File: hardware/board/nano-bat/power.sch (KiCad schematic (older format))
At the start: 26 parts, among them Q501 Q_PMOS_GSD, Q502 Q_NMOS_GSD, Q503 Q_NMOS_GSD, U501 MIC2104YML-TR, U502 MCP1702

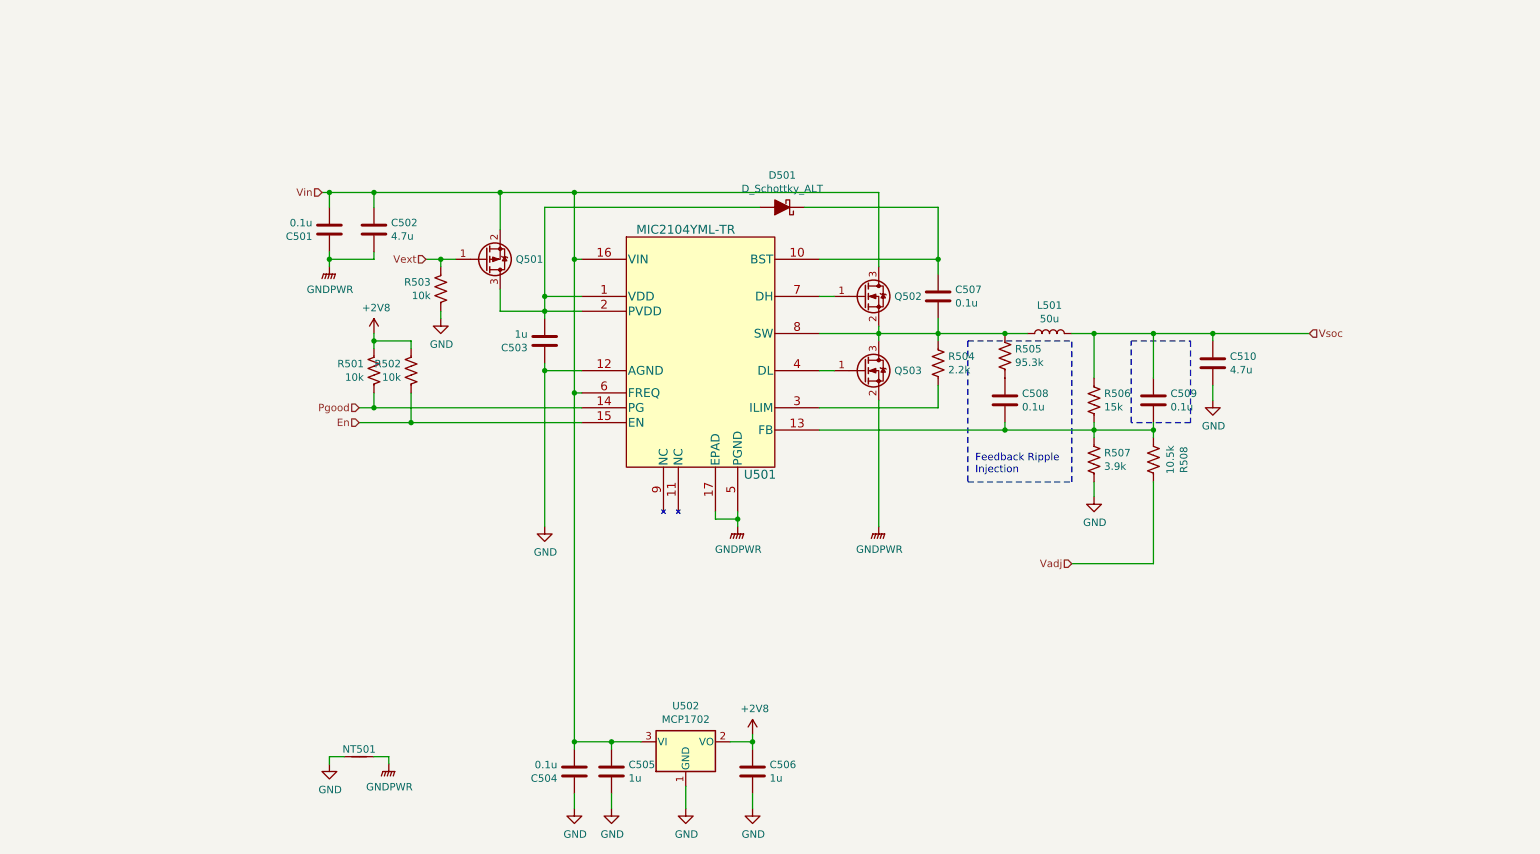
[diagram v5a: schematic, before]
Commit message: Adding docs to schematic
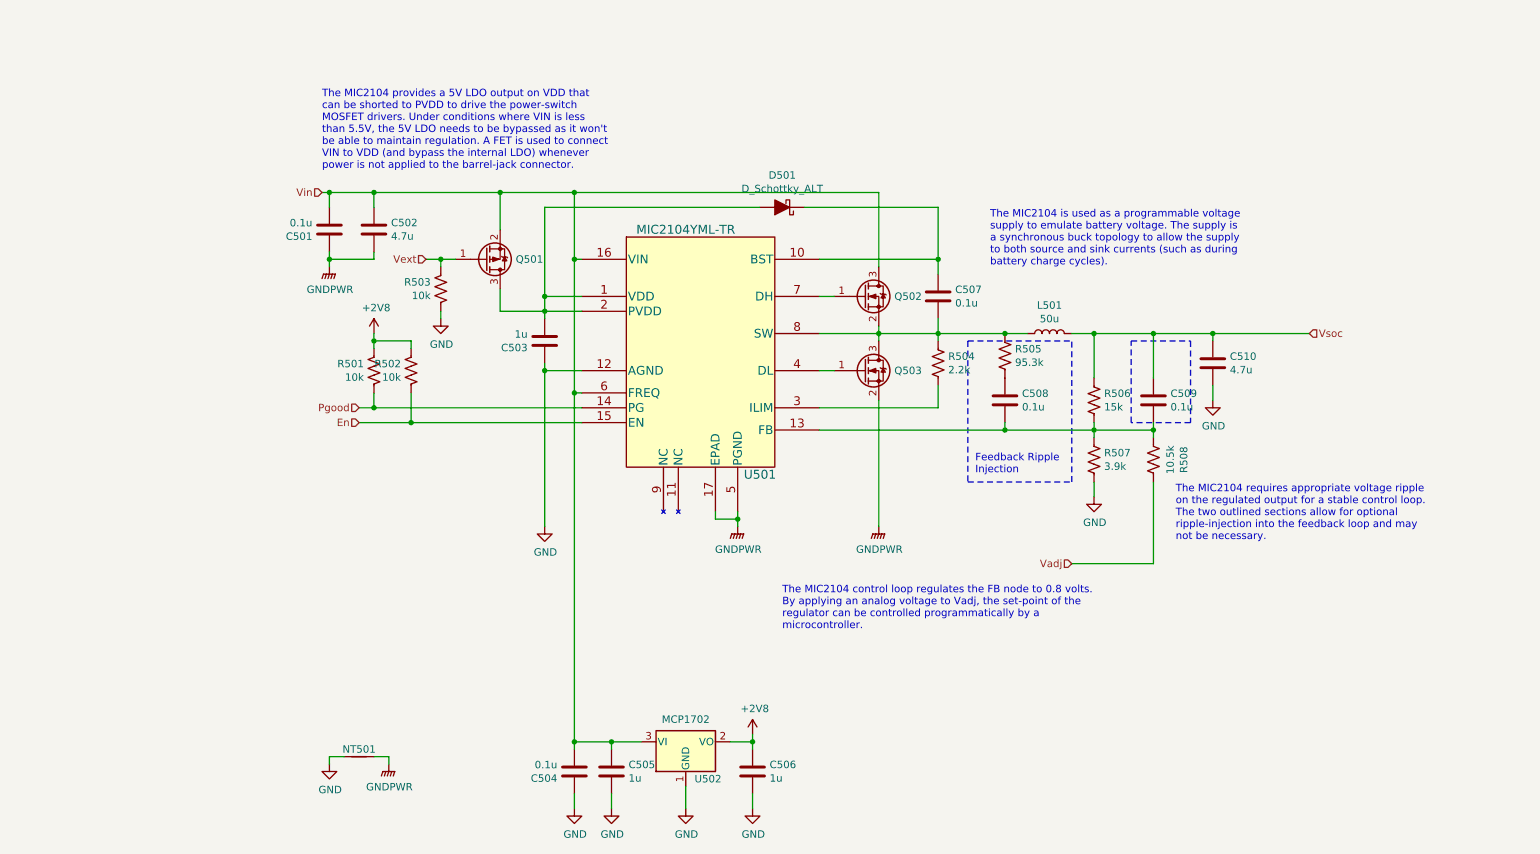
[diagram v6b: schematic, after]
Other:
- note added: "The MIC2104 control loop regulates the FB node to 0.8 volts. \nBy applying an analog voltage to Vadj, the set-point of the \nregulator can be controlled programmatically by a \nmicrocontroller."
- note added: "The MIC2104 is used as a programmable voltage \nsupply to emulate battery voltage. The supply is \na synchronous buck topology to allow the supply \nto both source and sink currents (such as during \nbattery charge cycles)."
- note added: "The MIC2104 provides a 5V LDO output on VDD that \ncan be shorted to PVDD to drive the power-switch \nMOSFET drivers. Under conditions where VIN is less \nthan 5.5V, the 5V LDO needs to be bypassed as it won't \nbe able to maintain regulation. A FET is used to connect \nVIN to VDD (and bypass the internal LDO) whenever \npower is not applied to the barrel-jack connector."
- note added: "The MIC2104 requires appropriate voltage ripple \non the regulated output for a stable control loop. \nThe two outlined sections allow for optional \nripple-injection into the feedback loop and may \nnot be necessary."
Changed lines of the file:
@@
 U 1 1 5DDCE1EA
 P 5400 5750
-F 0 "U502" H 5400 5992 50  0000 C CNN
+F 0 "U502" H 5550 5500 50  0000 C CNN
 F 1 "MCP1702" H 5400 5901 50  0000 C CNN
 F 2 "Package_TO_SOT_SMD:SOT-23" H 5400 5950 50  0001 C CNN
@@
 Wire Wire Line
 	4450 3250 4450 4300
+Text Notes 7450 2550 0    50   ~ 0
+The MIC2104 is used as a programmable voltage \nsupply to emulate battery voltage. The supply is \na synchronous buck topology to allow the supply \nto both source and sink currents (such as during \nbattery charge cycles).
+Text Notes 8700 4400 0    50   ~ 0
+The MIC2104 requires appropriate voltage ripple \non the regulated output for a stable control loop. \nThe two outlined sections allow for optional \nripple-injection into the feedback loop and may \nnot be necessary.
+Text Notes 6050 5000 0    50   ~ 0
+The MIC2104 control loop regulates the FB node to 0.8 volts. \nBy applying an analog voltage to Vadj, the set-point of the \nregulator can be controlled programmatically by a \nmicrocontroller.
+Text Notes 2950 1900 0    50   ~ 0
+The MIC2104 provides a 5V LDO output on VDD that \ncan be shorted to PVDD to drive the power-switch \nMOSFET drivers. Under conditions where VIN is less \nthan 5.5V, the 5V LDO needs to be bypassed as it won't \nbe able to maintain regulation. A FET is used to connect \nVIN to VDD (and bypass the internal LDO) whenever \npower is not applied to the barrel-jack connector.
 $EndSCHEMATC

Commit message: Adding 0.1.0 of board spin
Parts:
- removed C508, C509: 0.1u, Capacitor_SMD:C_0603_1608Metric, symbol Device:C
- removed D501: D_Schottky_ALT, Diode_SMD:D_SOD-323, symbol Device:D_Schottky_ALT
- removed NT501: Net-Tie_2, NetTie:NetTie-2_SMD_Pad2.0mm, symbol Device:Net-Tie_2
- removed Q501: Q_PMOS_GSD, Package_TO_SOT_SMD:SOT-23, symbol Device:Q_PMOS_GSD
- removed Q502, Q503: Q_NMOS_GSD, Package_TO_SOT_SMD:SOT-23, symbol Device:Q_NMOS_GSD
- removed R505: 95.3k, Resistor_SMD:R_0603_1608Metric, symbol Device:R_US
- removed R506: 15k, Resistor_SMD:R_0603_1608Metric, symbol Device:R_US
- removed R507: 3.9k, Resistor_SMD:R_0603_1608Metric, symbol Device:R_US
- removed R508: 10.5k, Resistor_SMD:R_0603_1608Metric, symbol Device:R_US
- removed U501: MIC2104YML-TR, Package_DFN_QFN:QFN-16-1EP_3x3mm_P0.5mm_EP1.7x1.7mm, symbol nano-bat:MIC2104YML-TR
- added F501: Polyfuse, Fuse:Fuse_1812_4532Metric, symbol Device:Polyfuse
- added U501: TPS562201, Package_TO_SOT_SMD:SOT-23-6, symbol Regulator_Switching:TPS562200
- C501, C507: value 0.1u -> 10u; footprint Capacitor_SMD:C_0603_1608Metric -> Capacitor_SMD:C_0805_2012Metric; Part 1276-1258-1-ND -> 399-3482-1-ND
- C502: value 4.7u -> 0.1u; Part 399-3482-1-ND -> 1276-1258-1-ND
- C503: value 1u -> 0.1u; Part 1276-1182-1-ND -> 1276-1258-1-ND
- C510: value 4.7u -> 10u; footprint Capacitor_SMD:C_0603_1608Metric -> Capacitor_SMD:C_0805_2012Metric
- L501: value 50u -> 4.7u; footprint footprints:NRS6028-IND-NS -> Inductor_SMD:L_Taiyo-Yuden_NR-60xx; Part 587-2942-1-ND -> 587-2100-1-ND
- R502: value 10k -> 1.96k; Part 311-10KGRCT-ND -> 311-1.96KHRCT-ND
- R503: value 10k -> 9.31k; Part 311-10KGRCT-ND -> RMCF0603FT9K31CT-ND
- R504: value 2.2k -> 10k; Part P2.2KGCT-ND -> 311-10.0KHRCT-ND
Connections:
- net Pgood is gone; now on net En: R501.2
- net +2V8: no longer R502.1
- net En: now also U501.5 (EN); no longer R502.2
- net GND: now also C501.2, C502.2, C507.2, R502.2, U501.1 (GND); no longer C503.1, R503.2
- net Vadj: now also R503.2
- net Vin: now also C501.1, U501.3 (VIN); no longer C501.2
- net Vsoc: now also F501.1; no longer C510.1, L501.2
- net at C503.2: now also L501.1, U501.2 (SW)
- net at C507.1: now also C510.1, L501.2, R504.2, F501.2
- removed net GNDPWR: C501.1, C502.2
- net Vext: no longer names the net of R503.1
- net Vext: now also R502.1, R504.1, U501.4 (VFB)
- new net: C503.1, U501.6 (VBST)
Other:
- note added: "Vsoc = 5.51 - (1.0741) * Vadj"
- note added: "Vsoc is adjusted to bias VFB to 0.768V. \nVadj is used to change the bias set-point \nthrough external analog control.\n"
- note removed: "Feedback Ripple\nInjection"
- note removed: "The MIC2104 control loop regulates the FB node to 0.8 volts. \nBy applying an analog voltage to Vadj, the set-point of the \nregulator can be controlled programmatically by a \nmicrocontroller."
- note removed: "The MIC2104 is used as a programmable voltage \nsupply to emulate battery voltage. The supply is \na synchronous buck topology to allow the supply \nto both source and sink currents (such as during \nbattery charge cycles)."
- note removed: "The MIC2104 provides a 5V LDO output on VDD that \ncan be shorted to PVDD to drive the power-switch \nMOSFET drivers. Under conditions where VIN is less \nthan 5.5V, the 5V LDO needs to be bypassed as it won't \nbe able to maintain regulation. A FET is used to connect \nVIN to VDD (and bypass the internal LDO) whenever \npower is not applied to the barrel-jack connector."
- note removed: "The MIC2104 requires appropriate voltage ripple \non the regulated output for a stable control loop. \nThe two outlined sections allow for optional \nripple-injection into the feedback loop and may \nnot be necessary."
- moved on the sheet: C510

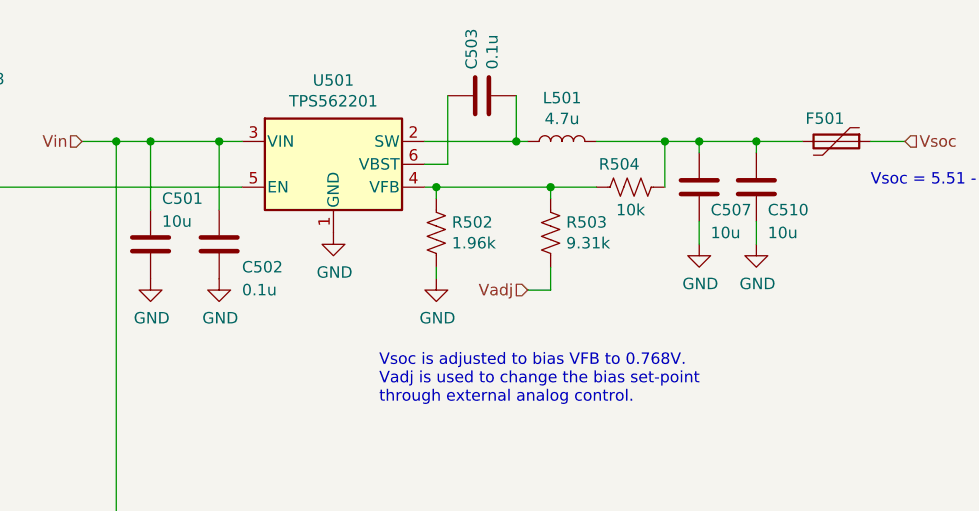
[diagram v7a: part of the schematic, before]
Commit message: Fixing schematic symbol sizes
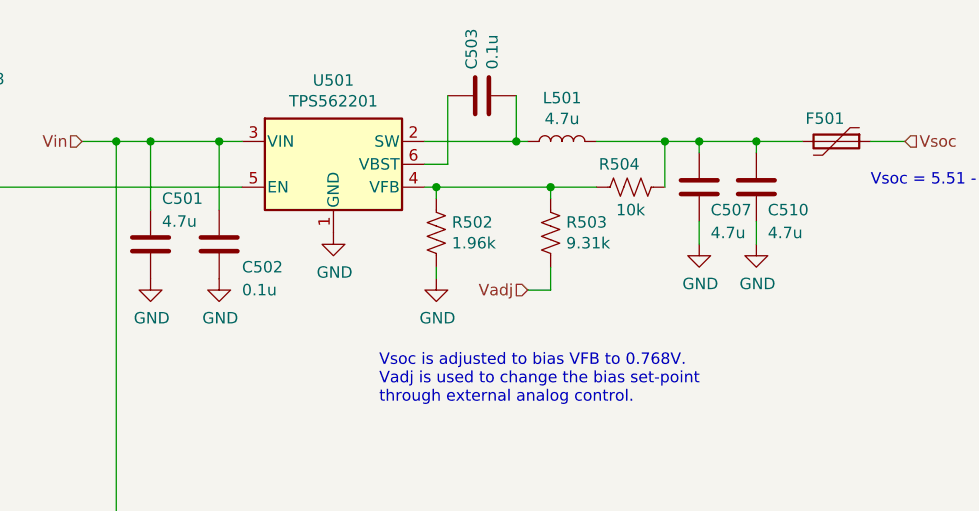
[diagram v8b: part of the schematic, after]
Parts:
- C501, C507, C510: value 10u -> 4.7u
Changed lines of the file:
@@
 P 7450 4050
 F 0 "C510" H 7500 3950 50  0000 L CNN
-F 1 "10u" H 7500 3850 50  0000 L CNN
+F 1 "4.7u" H 7500 3850 50  0000 L CNN
 F 2 "Capacitor_SMD:C_0805_2012Metric" H 7488 3900 50  0001 C CNN
 F 3 "~" H 7450 4050 50  0001 C CNN
@@
 P 7200 4050
 F 0 "C507" H 7250 3950 50  0000 L CNN
-F 1 "10u" H 7250 3850 50  0000 L CNN
+F 1 "4.7u" H 7250 3850 50  0000 L CNN
 F 2 "Capacitor_SMD:C_0805_2012Metric" H 7238 3900 50  0001 C CNN
 F 3 "~" H 7200 4050 50  0001 C CNN
@@
 P 4800 4300
 F 0 "C501" H 4850 4500 50  0000 L CNN
-F 1 "10u" H 4850 4400 50  0000 L CNN
+F 1 "4.7u" H 4850 4400 50  0000 L CNN
 F 2 "Capacitor_SMD:C_0805_2012Metric" H 4838 4150 50  0001 C CNN
 F 3 "~" H 4800 4300 50  0001 C CNN
